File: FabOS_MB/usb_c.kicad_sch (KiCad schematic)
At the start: 0 parts

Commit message: Sous module USB_C
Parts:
- added J2: USB_C_Receptacle, Librairie_MB:USB_C_femelle_12P, symbol Connector:USB_C_Receptacle
- added R1, R2: 5.1k, Resistor_SMD:R_0402_1005Metric, symbol Device:R_Small
- added U4: USBLC6-2SC6, Package_TO_SOT_SMD:SOT-23-6, symbol Power_Protection:USBLC6-2SC6
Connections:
- new net: J2.A5 (CC1), R1.1
- new net: J2.B5 (CC2), R2.1
- new net D+: J2.A6 (D+), J2.B6 (D+), U4.1 (I/O1)
- new net D-: J2.A7 (D-), J2.B7 (D-), U4.6 (I/O1)
- new net GND: J2.A1 (GND), J2.A12 (GND), J2.B1 (GND), J2.B12 (GND), J2.S1 (SHIELD), R1.2, R2.2, U4.2 (GND)
- new net USB_BOOT_DM: U4.4 (I/O2)
- new net USB_BOOT_DP: U4.3 (I/O2)
- new net V_USB: J2.A4 (VBUS), J2.A9 (VBUS), J2.B4 (VBUS), J2.B9 (VBUS), U4.5 (VBUS)
- no-connect marks 0 -> 2
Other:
- note added: "Valeurs des résistances prises avec le projet S6. Est-il nécessaire de les changer ? Schéma fait à partir du projet S6"

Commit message: Début LIN
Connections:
- net V_USB renamed VBUS
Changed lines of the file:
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@@
 		)
 	)
-	(hierarchical_label "V_USB"
+	(hierarchical_label "VBUS"
 		(shape input)
 		(at 189.23 78.74 90)
@@
 		)
 	)
-	(hierarchical_label "V_USB"
+	(hierarchical_label "VBUS"
 		(shape input)
 		(at 137.16 74.93 0)

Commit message: Schéma LIN
Je n'ai pas compris comment l'alim fonctionne
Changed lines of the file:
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@@
 	)
 	(hierarchical_label "USB_BOOT_DM"
-		(shape input)
+		(shape bidirectional)
 		(at 194.31 86.36 0)
 		(fields_autoplaced yes)
@@
 	)
 	(hierarchical_label "USB_BOOT_DP"
-		(shape input)
+		(shape bidirectional)
 		(at 184.15 86.36 180)
 		(fields_autoplaced yes)

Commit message: Maj schéma
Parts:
- renumbered R1 to R30, R2 to R31, U4 to U8
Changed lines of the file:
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@@
 		(instances
 			(project "FabOS_MB"
-				(path "/09377d5d-727f-4ff4-92c8-7a0483d23f1e/255e55c2-c856-4827-a81b-b3f46d86ff9a"
+				(path "/09377d5d-727f-4ff4-92c8-7a0483d23f1e/7da4f56f-ad27-4eb1-a317-8d2e7594465d"
 					(reference "J2")
 					(unit 1)
@@
 		(dnp no)
 		(fields_autoplaced yes)
-		(property "Reference" "R1"
+		(property "Reference" "R30"
 			(at 149.225 74.93 0)
 			(effects
@@
 		(instances
 			(project "FabOS_MB"
-				(path "/09377d5d-727f-4ff4-92c8-7a0483d23f1e/255e55c2-c856-4827-a81b-b3f46d86ff9a"
-					(reference "R1")
+				(path "/09377d5d-727f-4ff4-92c8-7a0483d23f1e/7da4f56f-ad27-4eb1-a317-8d2e7594465d"
+					(reference "R30")
 					(unit 1)
 				)
@@
 		(dnp no)
 		(fields_autoplaced yes)
-		(property "Reference" "R2"
+		(property "Reference" "R31"
 			(at 149.225 82.55 0)
 			(effects
@@
 		(instances
 			(project "FabOS_MB"
-				(path "/09377d5d-727f-4ff4-92c8-7a0483d23f1e/255e55c2-c856-4827-a81b-b3f46d86ff9a"
-					(reference "R2")
+				(path "/09377d5d-727f-4ff4-92c8-7a0483d23f1e/7da4f56f-ad27-4eb1-a317-8d2e7594465d"
+					(reference "R31")
 					(unit 1)
 				)
@@
 		(dnp no)
 		(fields_autoplaced yes)
-		(property "Reference" "#PWR02"
+		(property "Reference" "#PWR035"
 			(at 118.11 125.73 0)
 			(effects
@@
 		)
 		(instances
-			(project ""
-				(path "/09377d5d-727f-4ff4-92c8-7a0483d23f1e/255e55c2-c856-4827-a81b-b3f46d86ff9a"
-					(reference "#PWR02")
+			(project "FabOS_MB"
+				(path "/09377d5d-727f-4ff4-92c8-7a0483d23f1e/7da4f56f-ad27-4eb1-a317-8d2e7594465d"
+					(reference "#PWR035")
 					(unit 1)
 				)
@@
 		(dnp no)
 		(fields_autoplaced yes)
-		(property "Reference" "#PWR03"
+		(property "Reference" "#PWR037"
 			(at 189.23 97.79 0)
 			(effects
@@
 		)
 		(instances
-			(project ""
-				(path "/09377d5d-727f-4ff4-92c8-7a0483d23f1e/255e55c2-c856-4827-a81b-b3f46d86ff9a"
-					(reference "#PWR03")
+			(project "FabOS_MB"
+				(path "/09377d5d-727f-4ff4-92c8-7a0483d23f1e/7da4f56f-ad27-4eb1-a317-8d2e7594465d"
+					(reference "#PWR037")
 					(unit 1)
 				)
@@
 		(dnp no)
 		(fields_autoplaced yes)
-		(property "Reference" "#PWR01"
+		(property "Reference" "#PWR036"
 			(at 161.29 81.28 0)
 			(effects
@@
 		(instances
 			(project "FabOS_MB"
-				(path "/09377d5d-727f-4ff4-92c8-7a0483d23f1e/255e55c2-c856-4827-a81b-b3f46d86ff9a"
-					(reference "#PWR01")
+				(path "/09377d5d-727f-4ff4-92c8-7a0483d23f1e/7da4f56f-ad27-4eb1-a317-8d2e7594465d"
+					(reference "#PWR036")
 					(unit 1)
 				)
@@
 		(dnp no)
 		(fields_autoplaced yes)
-		(property "Reference" "U4"
+		(property "Reference" "U8"
 			(at 190.8811 76.2 0)
 			(effects
@@
 		(instances
 			(project "FabOS_MB"
-				(path "/09377d5d-727f-4ff4-92c8-7a0483d23f1e/255e55c2-c856-4827-a81b-b3f46d86ff9a"
-					(reference "U4")
-					(unit 1)
-				)
+				(path "/09377d5d-727f-4ff4-92c8-7a0483d23f1e/7da4f56f-ad27-4eb1-a317-8d2e7594465d"
+					(reference "U8")
+					(unit 1)
+				)

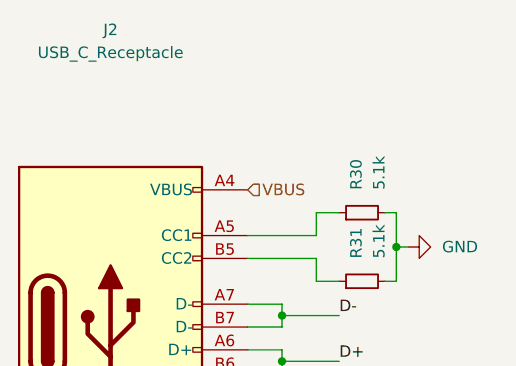
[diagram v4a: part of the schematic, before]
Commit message: ajout nom des composants pour 5v
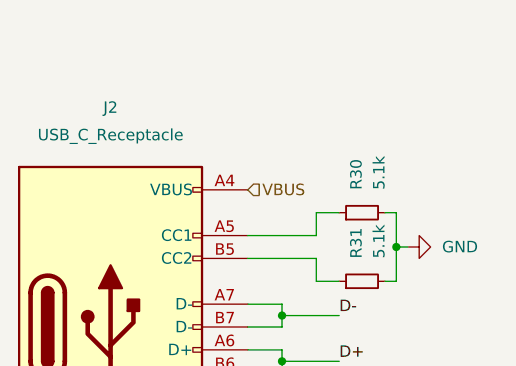
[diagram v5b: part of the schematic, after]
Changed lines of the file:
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@@
 		(on_board yes)
 		(dnp no)
-		(fields_autoplaced yes)
 		(property "Reference" "J2"
-			(at 121.92 57.15 0)
+			(at 121.92 65.786 0)
 			(effects
 				(font
@@
 		)
 		(property "Value" "USB_C_Receptacle"
-			(at 121.92 59.69 0)
+			(at 121.92 68.834 0)
 			(effects
 				(font

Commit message: Correction de certaines erreurs
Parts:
- renumbered R30 to R26, R31 to R27, U8 to U6
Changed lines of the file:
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@@
 		(dnp no)
 		(fields_autoplaced yes)
-		(property "Reference" "R30"
+		(property "Reference" "R26"
 			(at 149.225 74.93 0)
 			(effects
@@
 			(project "FabOS_MB"
 				(path "/09377d5d-727f-4ff4-92c8-7a0483d23f1e/7da4f56f-ad27-4eb1-a317-8d2e7594465d"
-					(reference "R30")
+					(reference "R26")
 					(unit 1)
 				)
@@
 		(dnp no)
 		(fields_autoplaced yes)
-		(property "Reference" "R31"
+		(property "Reference" "R27"
 			(at 149.225 82.55 0)
 			(effects
@@
 			(project "FabOS_MB"
 				(path "/09377d5d-727f-4ff4-92c8-7a0483d23f1e/7da4f56f-ad27-4eb1-a317-8d2e7594465d"
-					(reference "R31")
+					(reference "R27")
 					(unit 1)
 				)
@@
 		(dnp no)
 		(fields_autoplaced yes)
-		(property "Reference" "#PWR035"
+		(property "Reference" "#PWR037"
 			(at 118.11 125.73 0)
 			(effects
@@
 			(project "FabOS_MB"
 				(path "/09377d5d-727f-4ff4-92c8-7a0483d23f1e/7da4f56f-ad27-4eb1-a317-8d2e7594465d"
-					(reference "#PWR035")
+					(reference "#PWR037")
 					(unit 1)
 				)
@@
 		(dnp no)
 		(fields_autoplaced yes)
-		(property "Reference" "#PWR037"
+		(property "Reference" "#PWR039"
 			(at 189.23 97.79 0)
 			(effects
@@
 			(project "FabOS_MB"
 				(path "/09377d5d-727f-4ff4-92c8-7a0483d23f1e/7da4f56f-ad27-4eb1-a317-8d2e7594465d"
-					(reference "#PWR037")
+					(reference "#PWR039")
 					(unit 1)
 				)
@@
 		(dnp no)
 		(fields_autoplaced yes)
-		(property "Reference" "#PWR036"
+		(property "Reference" "#PWR038"
 			(at 161.29 81.28 0)
 			(effects
@@
 			(project "FabOS_MB"
 				(path "/09377d5d-727f-4ff4-92c8-7a0483d23f1e/7da4f56f-ad27-4eb1-a317-8d2e7594465d"
-					(reference "#PWR036")
+					(reference "#PWR038")
 					(unit 1)
 				)
@@
 		(dnp no)
 		(fields_autoplaced yes)
-		(property "Reference" "U8"
+		(property "Reference" "U6"
 			(at 190.8811 76.2 0)
 			(effects
@@
 			(project "FabOS_MB"
 				(path "/09377d5d-727f-4ff4-92c8-7a0483d23f1e/7da4f56f-ad27-4eb1-a317-8d2e7594465d"
-					(reference "U8")
-					(unit 1)
-				)
+					(reference "U6")
+					(unit 1)
+				)

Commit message: update pcb
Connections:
- net D-: now also U6.3 (I/O2); no longer U6.6 (I/O1)
- net USB_BOOT_DP: now also U6.6 (I/O1); no longer U6.3 (I/O2)
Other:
- moved on the sheet: U6
